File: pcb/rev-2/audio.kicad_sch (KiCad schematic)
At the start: 21 parts, among them J4 B5B-PH-K-S, U5 D3V3F4U6S-7, U6 TLV320ADC6120IRTER

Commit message: pcb: full rev-2 layout
Mostly finished layout for the rev-2 board
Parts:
- C16, C17, C18, C19: manf# FCA1206A105M-H3 -> 885012208093
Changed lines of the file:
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@@
 			)
 		)
-		(property "Datasheet" "https://www.cde.com/resources/catalogs/FCA.pdf"
+		(property "Datasheet" "https://www.we-online.com/components/products/datasheet/885012208093.pdf"
 			(at 63.5 64.77 0)
 			(effects
@@
 			)
 		)
-		(property "Description" "Film Capacitor 12V 10V Acrylic, Metallized 1206 (3216 Metric)"
+		(property "Description" "1 µF ±10% 50V Ceramic Capacitor X7R"
 			(at 63.5 64.77 0)
 			(effects
@@
 			)
 		)
-		(property "manf#" "FCA1206A105M-H3"
+		(property "manf#" "885012208093"
 			(at 63.5 64.77 90)
 			(effects
@@
 			)
 		)
-		(property "Datasheet" "https://www.cde.com/resources/catalogs/FCA.pdf"
+		(property "Datasheet" "https://www.we-online.com/components/products/datasheet/885012208093.pdf"
 			(at 63.5 76.2 0)
 			(effects
@@
 			)
 		)
-		(property "Description" "Film Capacitor 12V 10V Acrylic, Metallized 1206 (3216 Metric)"
+		(property "Description" "1 µF ±10% 50V Ceramic Capacitor X7R"
 			(at 63.5 76.2 0)
 			(effects
@@
 			)
 		)
-		(property "manf#" "FCA1206A105M-H3"
+		(property "manf#" "885012208093"
 			(at 63.5 76.2 90)
 			(effects
@@
 			)
 		)
-		(property "Datasheet" "https://www.cde.com/resources/catalogs/FCA.pdf"
+		(property "Datasheet" "https://www.we-online.com/components/products/datasheet/885012208093.pdf"
 			(at 63.5 88.9 0)
 			(effects
@@
 			)
 		)
-		(property "Description" "Film Capacitor 12V 10V Acrylic, Metallized 1206 (3216 Metric)"
+		(property "Description" "1 µF ±10% 50V Ceramic Capacitor X7R"
 			(at 63.5 88.9 0)
 			(effects
@@
 			)
 		)
-		(property "manf#" "FCA1206A105M-H3"
+		(property "manf#" "885012208093"
 			(at 63.5 88.9 90)
 			(effects
@@
 			)
 		)
-		(property "Datasheet" "https://www.cde.com/resources/catalogs/FCA.pdf"
+		(property "Datasheet" "https://www.we-online.com/components/products/datasheet/885012208093.pdf"
 			(at 63.5 101.6 0)
 			(effects
@@
 			)
 		)
-		(property "Description" "Film Capacitor 12V 10V Acrylic, Metallized 1206 (3216 Metric)"
+		(property "Description" "1 µF ±10% 50V Ceramic Capacitor X7R"
 			(at 63.5 101.6 0)
 			(effects
@@
 			)
 		)
-		(property "manf#" "FCA1206A105M-H3"
+		(property "manf#" "885012208093"
 			(at 63.5 101.6 90)
 			(effects

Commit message: pcb: minor schematic cleanup
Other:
- title: (none) -> ADC and input circuitry
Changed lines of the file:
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@@
 	(generator_version "8.0")
 	(paper "A4")
+	(title_block
+		(title "ADC and input circuitry")
+	)
 	(junction
 		(at 91.44 97.79)

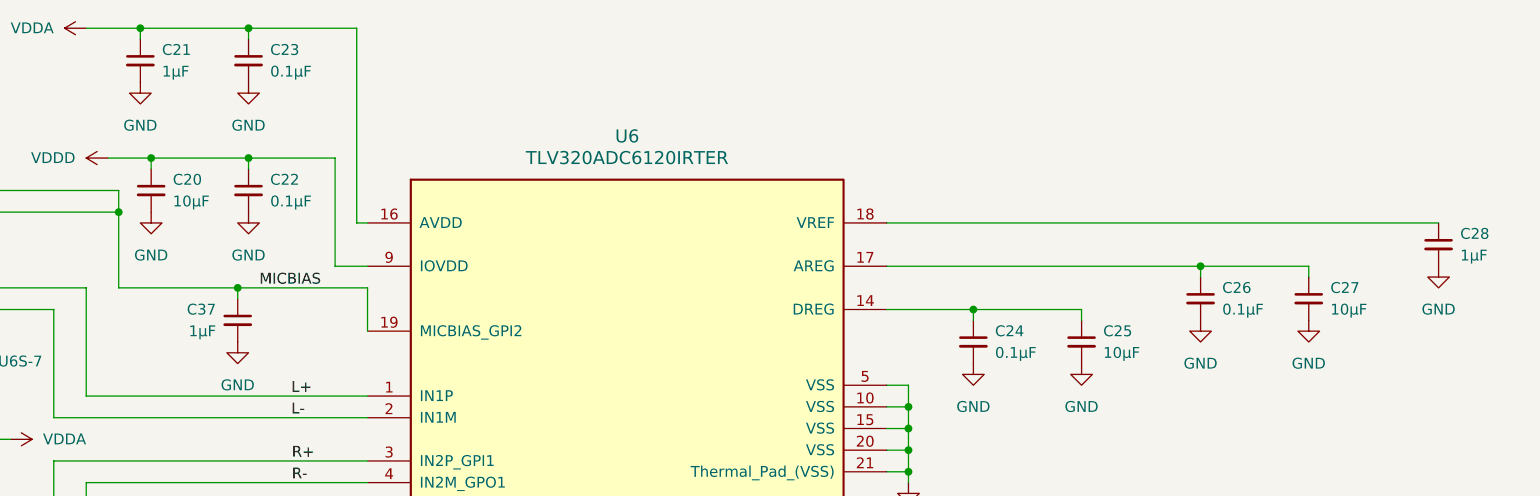
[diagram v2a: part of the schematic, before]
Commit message: pcb: update
Mostly downsize several decoupling capacitors to save space
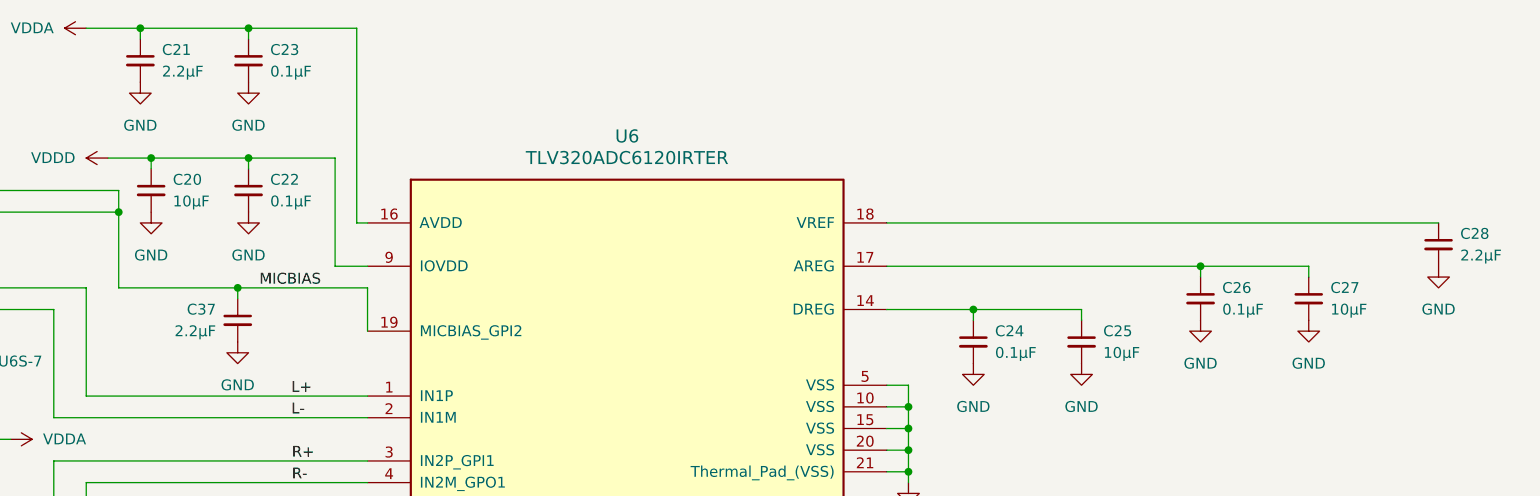
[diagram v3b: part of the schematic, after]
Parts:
- C21, C28, C37: value 1µF -> 2.2µF; footprint Capacitor_SMD:C_0603_1608Metric -> zeus-le:C_0402_1005Metric_Silkscreen_Clearance; manf# CL10B105KP8NNNC -> GRM155R61A225ME01D
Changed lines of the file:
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@@
 			)
 		)
-		(property "Value" "1µF"
+		(property "Value" "2.2µF"
 			(at 273.05 60.9662 0)
 			(effects
@@
 			)
 		)
-		(property "Footprint" "Capacitor_SMD:C_0603_1608Metric"
+		(property "Footprint" "zeus-le:C_0402_1005Metric_Silkscreen_Clearance"
 			(at 270.51 59.69 0)
 			(effects
@@
 			)
 		)
-		(property "Description" "Capacitor, decoupling, 10V, X7R"
+		(property "Description" "Capacitor, decoupling, 10V, X5R"
 			(at 270.51 59.69 0)
 			(effects
@@
 			)
 		)
-		(property "manf#" "CL10B105KP8NNNC"
+		(property "manf#" "GRM155R61A225ME01D"
 			(at 270.51 59.69 0)
 			(effects
@@
 			)
 		)
-		(property "Value" "1µF"
+		(property "Value" "2.2µF"
 			(at 120.65 39.3762 0)
 			(effects
@@
 			)
 		)
-		(property "Footprint" "Capacitor_SMD:C_0603_1608Metric"
+		(property "Footprint" "zeus-le:C_0402_1005Metric_Silkscreen_Clearance"
 			(at 118.11 38.1 0)
 			(effects
@@
 			)
 		)
-		(property "Description" "Capacitor, decoupling, 10V, X7R"
+		(property "Description" "Capacitor, decoupling, 10V, X5R"
 			(at 118.11 38.1 0)
 			(effects
@@
 			)
 		)
-		(property "manf#" "CL10B105KP8NNNC"
+		(property "manf#" "GRM155R61A225ME01D"
 			(at 118.11 38.1 0)
 			(effects
@@
 			)
 		)
-		(property "Value" "1µF"
+		(property "Value" "2.2µF"
 			(at 127 69.8562 0)
 			(effects
@@
 			)
 		)
-		(property "Footprint" "Capacitor_SMD:C_0603_1608Metric"
+		(property "Footprint" "zeus-le:C_0402_1005Metric_Silkscreen_Clearance"
 			(at 129.54 68.58 0)
 			(effects
@@
 			)
 		)
-		(property "Description" "Capacitor, decoupling, 10V, X7R"
+		(property "Description" "Capacitor, decoupling, 10V, X5R"
 			(at 129.54 68.58 0)
 			(effects
@@
 			)
 		)
-		(property "manf#" "CL10B105KP8NNNC"
+		(property "manf#" "GRM155R61A225ME01D"
 			(at 129.54 68.58 0)
 			(effects

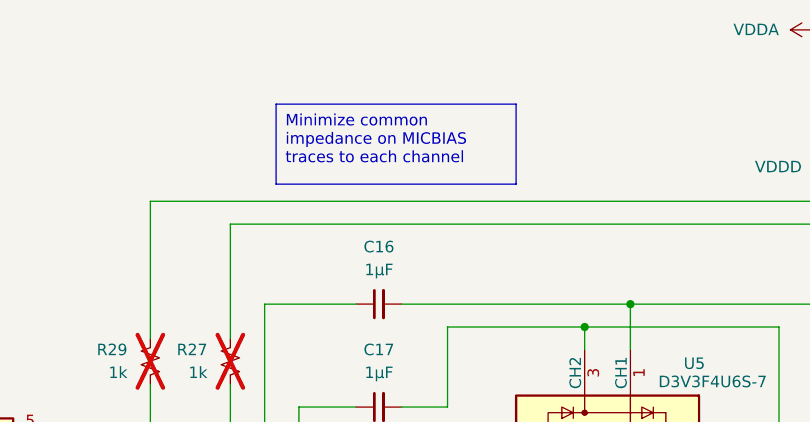
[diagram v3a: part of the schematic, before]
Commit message: pcb: upgrade to KiCad 9.0
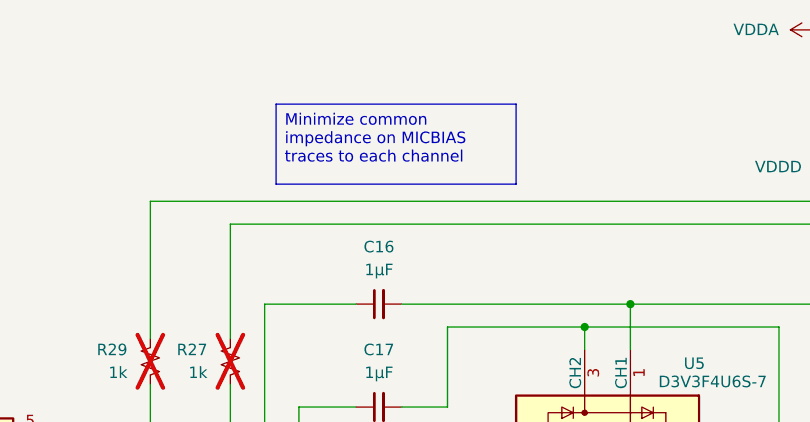
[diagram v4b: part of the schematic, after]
